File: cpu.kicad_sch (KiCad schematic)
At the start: 29 parts, among them J81 Conn_01x03_Pin, J82 Conn_Coaxial, J83 Conn_Coaxial, J84 Conn_01x02_Pin, SW81 SW_Push, SW82 SW_Push, U8 ESP32-C6-MINI-1U, U81 74HC595, U82 74HC595, U84 ISOW7842

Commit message: Put in some IO resistors.
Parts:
- added R91, R92: 100, Resistor_SMD:R_0402_1005Metric, symbol Device:R
- added R93, R94, R95, R96, R97, R98, R99: 33, Resistor_SMD:R_0402_1005Metric, symbol Device:R
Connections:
- net LATCH: now also R98.2; no longer U8.28 (IO22)
- net MOSI: now also R93.1; no longer U8.16 (IO7)
- net RX: now also R92.2; no longer U8.30 (RXD0)
- net TX: now also R91.2; no longer U8.31 (TXD0)
- net ~{CS2}: now also R94.2; no longer U8.24 (IO18)
- net ~{CS3}: now also R95.2; no longer U8.25 (IO19)
- net ~{CS4}: now also R96.2; no longer U8.26 (IO20)
- net ~{CS5}: now also R97.2; no longer U8.27 (IO21)
- net ~{LDAC}: now also R99.2; no longer U8.29 (IO23)
- new net: R97.1, U8.27 (IO21)
- new net: R93.2, U8.16 (IO7)
- new net: R94.1, U8.24 (IO18)
- new net: R99.1, U8.29 (IO23)
- new net: R91.1, U8.31 (TXD0)
- new net: R92.1, U8.30 (RXD0)
- new net: R98.1, U8.28 (IO22)
- new net: R96.1, U8.26 (IO20)
- new net: R95.1, U8.25 (IO19)
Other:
- moved on the sheet: J81, R90

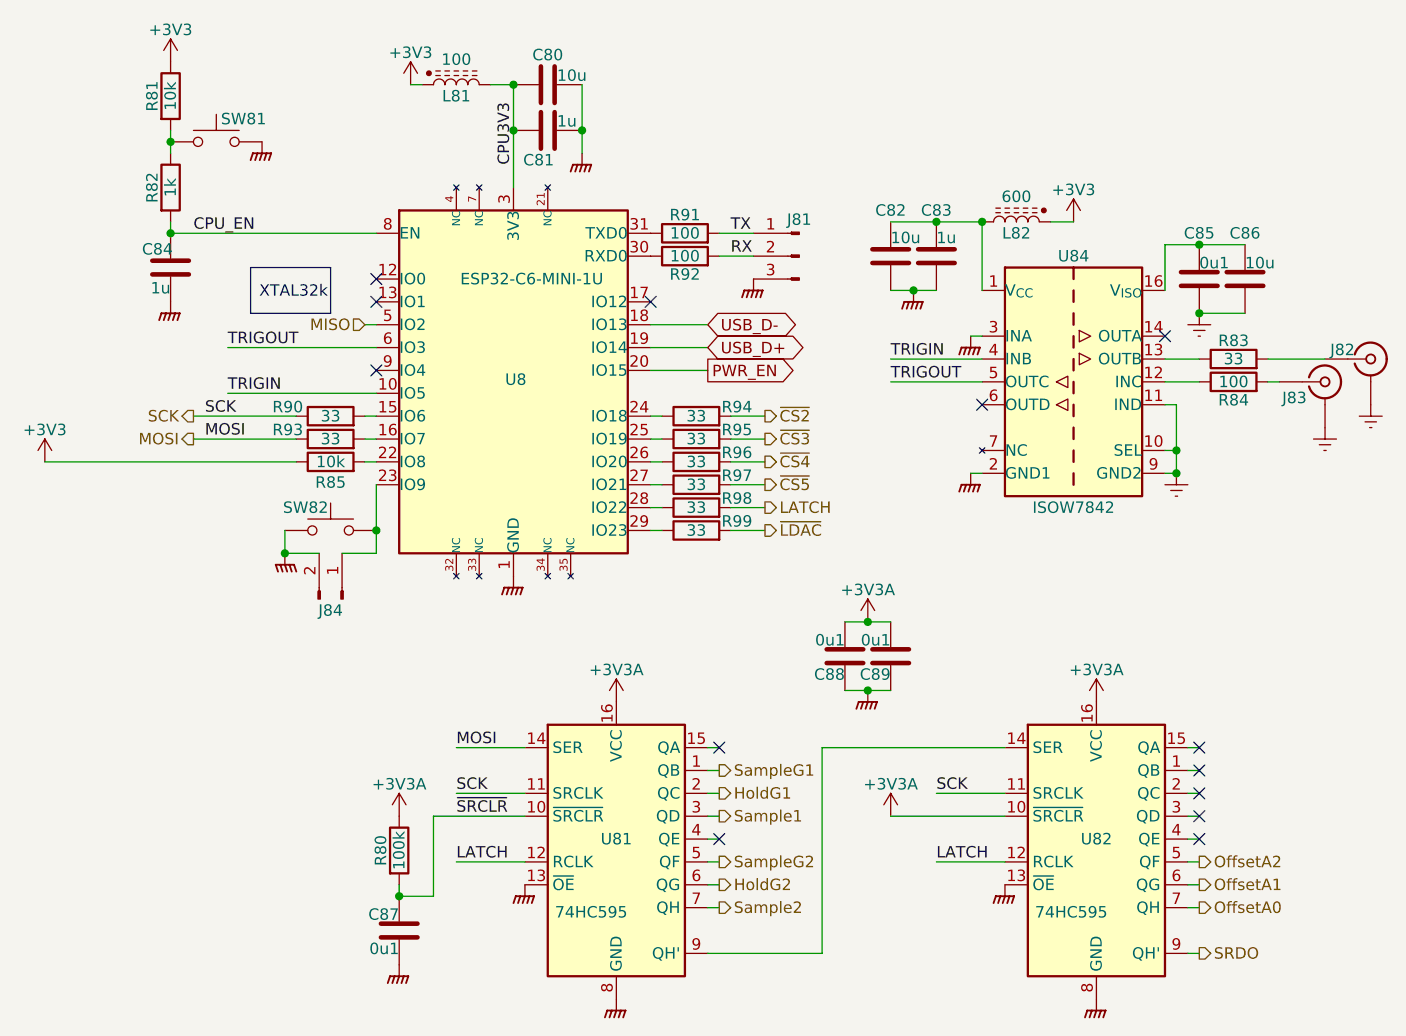
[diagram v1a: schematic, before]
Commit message: DRC update.  Repin ADC.  De-crack the S/H ground.
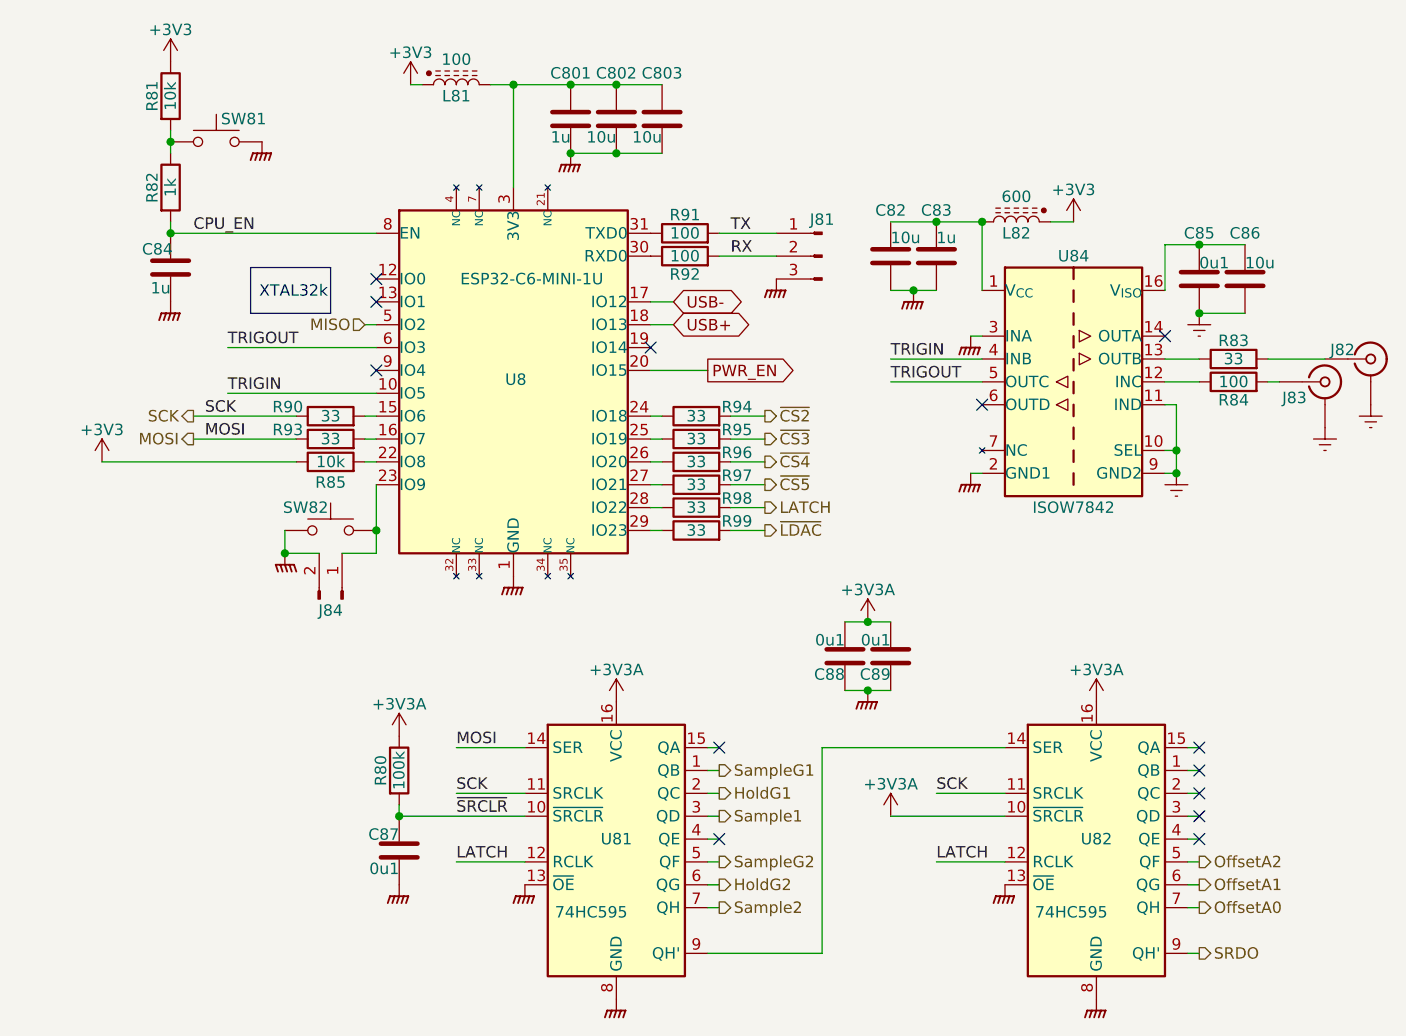
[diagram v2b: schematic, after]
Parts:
- added C803: 10u, Capacitor_SMD:C_0603_1608Metric, symbol Device:C
- renumbered C81 to C801, C80 to C802
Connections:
- net GNDPWR: now also C803.2
- net USB-: now reaches U8.17 (IO12)
- net CPU3V3: no longer names the net of C801.1, C802.1, L81.2, U8.3 (3V3)
- net CPU3V3: now also C803.1
- net USB_D+: no longer names the net of U8.19 (IO14)
- net USB_D- renamed USB+
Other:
- moved on the sheet: C801, C802, C87, J81, R80

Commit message: More component metadata.
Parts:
- C801, C802, C803, C82, C83, C84, C85, C86, C87, C88, C89, L81, L82, R80, R81, R82, R83, R84, R85, R90, R91, R92, R93, R94, R95, R96, R97, R98, R99, SW81, SW82, U8, U81, U82: Stock (none) -> JLC
- J81, J84: Stock (none) -> Heaps
- J82, J83: Stock (none) -> Bag
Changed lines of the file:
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@@
 			)
 		)
-		(property "Stock" ""
+		(property "Stock" "JLC"
 			(at 142.24 50.8 0)
 			(effects
@@
 			)
 		)
-		(property "Stock" ""
+		(property "Stock" "JLC"
 			(at 106.68 35.56 90)
 			(effects
@@
 			)
 		)
-		(property "Stock" ""
+		(property "Stock" "JLC"
 			(at 62.23 38.1 0)
 			(effects
@@
 			)
 		)
-		(property "Stock" ""
+		(property "Stock" "JLC"
 			(at 115.57 76.2 90)
 			(effects
@@
 			)
 		)
-		(property "Stock" ""
+		(property "Stock" "JLC"
 			(at 74.93 71.12 90)
 			(effects
@@
 			)
 		)
-		(property "Stock" ""
+		(property "Stock" "JLC"
 			(at 74.93 68.58 90)
 			(effects
@@
 			)
 		)
-		(property "Stock" ""
+		(property "Stock" "JLC"
 			(at 106.68 115.57 0)
 			(effects
@@
 			)
 		)
-		(property "Stock" ""
+		(property "Stock" "JLC"
 			(at 137.16 50.8 0)
 			(effects
@@
 			)
 		)
-		(property "Stock" ""
+		(property "Stock" "JLC"
 			(at 57.15 33.02 90)
 			(effects
@@
 			)
 		)
-		(property "Stock" ""
+		(property "Stock" "JLC"
 			(at 57.15 43.18 90)
 			(effects
@@
 			)
 		)
-		(property "Stock" ""
+		(property "Stock" "JLC"
 			(at 115.57 68.58 90)
 			(effects
@@
 			)
 		)
-		(property "Stock" ""
+		(property "Stock" "Bag"
 			(at 185.42 64.77 0)
 			(effects
@@
 			)
 		)
-		(property "Stock" ""
+		(property "Stock" "JLC"
 			(at 160.02 115.57 0)
 			(effects
@@
 			)
 		)
-		(property "Stock" ""
+		(property "Stock" "JLC"
 			(at 115.57 81.28 90)
 			(effects
@@
 			)
 		)
-		(property "Stock" ""
+		(property "Stock" "JLC"
 			(at 114.3 48.26 90)
 			(effects
@@
 			)
 		)
-		(property "Stock" ""
+		(property "Stock" "JLC"
 			(at 132.08 95.25 0)
 			(effects
@@
 			)
 		)
-		(property "Stock" ""
+		(property "Stock" "JLC"
 			(at 114.3 50.8 90)
 			(effects
@@
 			)
 		)
-		(property "Stock" ""
+		(property "Stock" "JLC"
 			(at 74.93 73.66 90)
 			(effects
@@
 			)
 		)
-		(property "Stock" ""
+		(property "Stock" "Bag"
 			(at 190.5 62.23 0)
 			(effects
@@
 			)
 		)
-		(property "Stock" ""
+		(property "Stock" "JLC"
 			(at 115.57 78.74 90)
 			(effects
@@
 			)
 		)
-		(property "Stock" ""
+		(property "Stock" "JLC"
 			(at 101.6 35.56 90)
 			(effects
@@
 			)
 		)
-		(property "Stock" ""
+		(property "Stock" "JLC"
 			(at 137.16 95.25 0)
 			(effects
@@
 			)
 		)
-		(property "Stock" ""
+		(property "Stock" "Heaps"
 			(at 129.54 50.8 0)
 			(effects
@@
 			)
 		)
-		(property "Stock" ""
+		(property "Stock" "JLC"
 			(at 175.26 62.23 90)
 			(effects
@@
 			)
 		)
-		(property "Stock" ""
+		(property "Stock" "JLC"
 			(at 115.57 73.66 90)
 			(effects
@@
 			)
 		)
-		(property "Stock" ""
+		(property "Stock" "JLC"
 			(at 57.15 52.07 0)
 			(effects
@@
 			)
 		)
-		(property "Stock" ""
+		(property "Stock" "JLC"
 			(at 74.93 81.28 0)
 			(effects
@@
 			)
 		)
-		(property "Stock" ""
+		(property "Stock" "JLC"
 			(at 171.45 53.34 0)
 			(effects
@@
 			)
 		)
-		(property "Stock" ""
+		(property "Stock" "Heaps"
 			(at 76.2 88.9 90)
 			(effects
@@
 			)
 		)
-		(property "Stock" ""
+		(property "Stock" "JLC"
 			(at 82.55 107.95 90)
 			(effects
@@
 			)
 		)
-		(property "Stock" ""
+		(property "Stock" "JLC"
 			(at 151.13 46.99 90)
 			(effects
@@
 			)
 		)
-		(property "Stock" ""
+		(property "Stock" "JLC"
 			(at 95.25 64.77 0)
 			(effects
@@
 			)
 		)
-		(property "Stock" ""
+		(property "Stock" "JLC"
 			(at 88.9 31.75 90)
 			(effects
@@
 			)
 		)
-		(property "Stock" ""
+		(property "Stock" "JLC"
 			(at 115.57 71.12 90)
 			(effects
@@
 			)
 		)
-		(property "Stock" ""
+		(property "Stock" "JLC"
 			(at 176.53 53.34 0)
 			(effects
@@
 			)
 		)
-		(property "Stock" ""
+		(property "Stock" "JLC"
 			(at 82.55 116.84 0)
 			(effects
@@
 			)
 		)
-		(property "Stock" ""
+		(property "Stock" "JLC"
 			(at 111.76 35.56 90)
 			(effects
@@
 			)
 		)
-		(property "Stock" ""
+		(property "Stock" "JLC"
 			(at 175.26 64.77 90)
 			(effects

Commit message: Front panel
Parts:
- added D81, D82: LED, LED_SMD:LED_0805_2012Metric, symbol Device:LED
- added R801, R802: 2k2, Resistor_SMD:R_0603_1608Metric, symbol Device:R
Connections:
- net GNDPWR: now also D81.1 (K), D82.1 (K)
- net PWR_EN: now also U8.19 (IO14); no longer U8.20 (IO15)
- net TRIGIN: now also U84.5 (OUTC); no longer U84.4 (INB)
- net TRIGOUT: now also U84.4 (INB); no longer U84.5 (OUTC)
- net Green: now reaches U8.12 (IO0)
- net Green: now also R802.1
- net SYNCMON: now reaches U8.9 (IO4)
- new net: D82.2 (A), R802.2
- new net: D81.2 (A), R801.2
- new net White: R801.1, U8.20 (IO15)
- no-connect marks 13 -> 10
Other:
- moved on the sheet: C87, R80, U81, U82

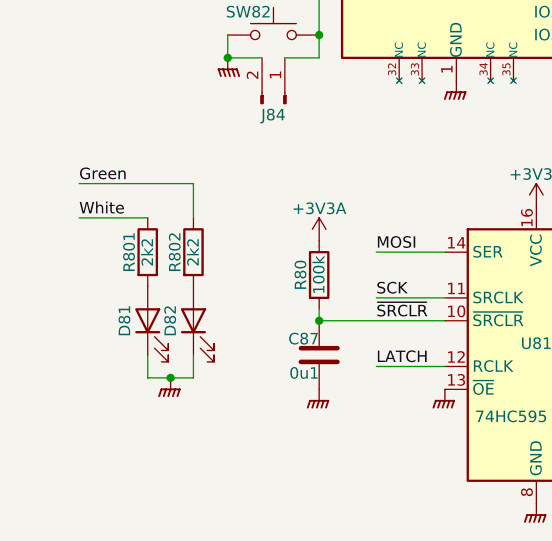
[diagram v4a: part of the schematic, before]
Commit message: Protection on ground drives.
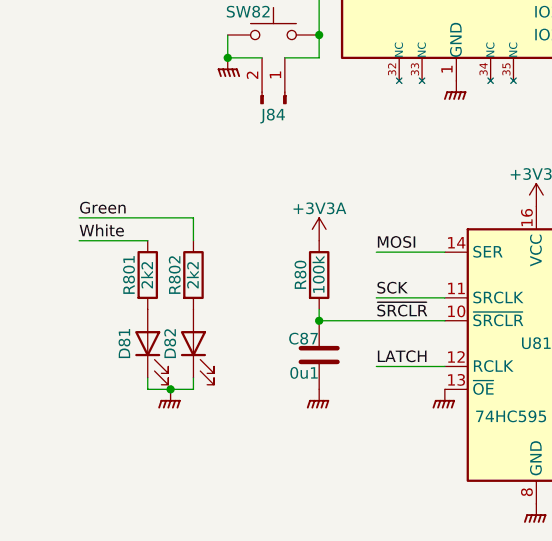
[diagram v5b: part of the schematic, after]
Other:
- moved on the sheet: D81, D82, R801, R802
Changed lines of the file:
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@@
 	)
 	(junction
-		(at 63.5 119.38)
+		(at 63.5 120.65)
 		(diameter 0)
 		(color 0 0 0 0)
@@
 	(wire
 		(pts
-			(xy 60.96 101.6) (xy 53.34 101.6)
-		)
-		(stroke
-			(width 0)
-			(type default)
-		)
-	)
-	(wire
-		(pts
 			(xy 119.38 71.12) (xy 123.19 71.12)
 		)
@@
 	(wire
 		(pts
-			(xy 53.34 97.79) (xy 66.04 97.79)
+			(xy 53.34 101.6) (xy 66.04 101.6)
 		)
 		(stroke
@@
 	(wire
 		(pts
-			(xy 60.96 119.38) (xy 63.5 119.38)
+			(xy 60.96 120.65) (xy 63.5 120.65)
 		)
 		(stroke
@@
 	(wire
 		(pts
-			(xy 66.04 116.84) (xy 66.04 119.38)
+			(xy 66.04 119.38) (xy 66.04 120.65)
 		)
 		(stroke
@@
 	(wire
 		(pts
-			(xy 63.5 119.38) (xy 66.04 119.38)
+			(xy 63.5 120.65) (xy 66.04 120.65)
 		)
 		(stroke
@@
 	(wire
 		(pts
-			(xy 66.04 101.6) (xy 66.04 97.79)
+			(xy 66.04 104.14) (xy 66.04 101.6)
 		)
 		(stroke
@@
 	(wire
 		(pts
+			(xy 53.34 104.14) (xy 60.96 104.14)
+		)
+		(stroke
+			(width 0)
+			(type default)
+		)
+	)
+	(wire
+		(pts
 			(xy 114.3 123.19) (xy 115.57 123.19)
 		)
@@
 	(wire
 		(pts
-			(xy 60.96 116.84) (xy 60.96 119.38)
+			(xy 60.96 119.38) (xy 60.96 120.65)
 		)
 		(stroke
@@
 	)
 	(label "White"
-		(at 53.34 101.6 0)
+		(at 53.34 104.14 0)
 		(effects
 			(font
@@
 	)
 	(label "Green"
-		(at 53.34 97.79 0)
+		(at 53.34 101.6 0)
 		(effects
 			(font
@@
 	(symbol
 		(lib_id "Device:LED")
-		(at 66.04 113.03 90)
+		(at 66.04 115.57 90)
 		(unit 1)
 		(exclude_from_sim no)
@@
 		(dnp no)
 		(property "Reference" "D82"
-			(at 63.5 113.03 0)
+			(at 63.5 115.57 0)
 			(effects
 				(font
@@
 		)
 		(property "Value" "LED"
-			(at 68.58 113.03 0)
+			(at 68.58 115.57 0)
 			(effects
 				(font
@@
 		)
 		(property "Footprint" "LED_SMD:LED_0805_2012Metric"
-			(at 66.04 113.03 0)
+			(at 66.04 115.57 0)
 			(effects
 				(font
@@
 		)
 		(property "Datasheet" "Green"
-			(at 66.04 113.03 0)
+			(at 66.04 115.57 0)
 			(effects
 				(font
@@
 		)
 		(property "Description" "Light emitting diode"
-			(at 66.04 113.03 0)
+			(at 66.04 115.57 0)
 			(effects
 				(font
@@
 		)
 		(property "Sim.Pins" "1=K 2=A"
-			(at 66.04 113.03 0)
+			(at 66.04 115.57 0)
 			(effects
 				(font
@@
 		)
 		(property "LCSC" "C2297"
-			(at 66.04 113.03 0)
+			(at 66.04 115.57 0)
 			(effects
 				(font
@@
 		)
 		(property "Stock" "JLC"
-			(at 66.04 113.03 0)
+			(at 66.04 115.57 0)
 			(effects
 				(font
@@
 	(symbol
 		(lib_id "Device:R")
-		(at 66.04 105.41 0)
+		(at 66.04 107.95 0)
 		(unit 1)
 		(exclude_from_sim no)
@@
 		(dnp no)
 		(property "Reference" "R802"
-			(at 64.008 105.41 90)
+			(at 64.008 107.95 90)
 			(effects
 				(font
@@
 		)
 		(property "Value" "2k2"
-			(at 66.04 105.41 90)
+			(at 66.04 107.95 90)
 			(effects
 				(font
@@
 		)
 		(property "Footprint" "Resistor_SMD:R_0603_1608Metric"
-			(at 64.262 105.41 90)
+			(at 64.262 107.95 90)
 			(effects
 				(font
@@
 		)
 		(property "Datasheet" "~"
-			(at 66.04 105.41 0)
+			(at 66.04 107.95 0)
 			(effects
 				(font
@@
 		)
 		(property "Description" "Resistor"
-			(at 66.04 105.41 0)
+			(at 66.04 107.95 0)
 			(effects
 				(font
@@
 		)
 		(property "LCSC" "C4190"
-			(at 66.04 105.41 90)
+			(at 66.04 107.95 90)
 			(effects
 				(font
@@
 		)
 		(property "Stock" "JLC"
-			(at 66.04 105.41 90)
+			(at 66.04 107.95 90)
 			(effects
 				(font
@@
 	(symbol
 		(lib_id "power:GNDPWR")
-		(at 63.5 119.38 0)
+		(at 63.5 120.65 0)
 		(unit 1)
 		(exclude_from_sim no)
@@
 		(dnp no)
 		(property "Reference" "#PWR0770"
-			(at 63.5 125.73 0)
+			(at 63.5 127 0)
 			(effects
 				(font
@@
 		)
 		(property "Value" "GNDPWR"
-			(at 63.5 122.682 0)
+			(at 63.5 123.952 0)
 			(effects
 				(font
@@
 		)
 		(property "Footprint" ""
-			(at 63.5 120.65 0)
+			(at 63.5 121.92 0)
 			(effects
 				(font
@@
 		)
 		(property "Datasheet" "~"
-			(at 63.5 120.65 0)
+			(at 63.5 121.92 0)
 			(effects
 				(font
@@
 		)
 		(property "Description" "Power symbol creates a global label with name \"GNDPWR\" , global ground"
-			(at 63.5 119.38 0)
+			(at 63.5 120.65 0)
 			(effects
 				(font
@@
 	(symbol
 		(lib_id "Device:LED")
-		(at 60.96 113.03 90)
+		(at 60.96 115.57 90)
 		(unit 1)
 		(exclude_from_sim no)
@@
 		(dnp no)
 		(property "Reference" "D81"
-			(at 58.42 113.03 0)
+			(at 58.42 115.57 0)
 			(effects
 				(font
@@
 		)
 		(property "Value" "LED"
-			(at 63.5 113.03 0)
+			(at 63.5 115.57 0)
 			(effects
 				(font
@@
 		)
 		(property "Footprint" "LED_SMD:LED_0805_2012Metric"
-			(at 60.96 113.03 0)
+			(at 60.96 115.57 0)
 			(effects
 				(font
@@
 		)
 		(property "Datasheet" "White"
-			(at 60.96 113.03 0)
+			(at 60.96 115.57 0)
 			(effects
 				(font
@@
 		)
 		(property "Description" "Light emitting diode"
-			(at 60.96 113.03 0)
+			(at 60.96 115.57 0)
 			(effects
 				(font
@@
 		)
 		(property "Sim.Pins" "1=K 2=A"
-			(at 60.96 113.03 0)
+			(at 60.96 115.57 0)
 			(effects
 				(font
@@
 		)
 		(property "LCSC" "C34499"
-			(at 60.96 113.03 0)
+			(at 60.96 115.57 0)
 			(effects
 				(font
@@
 		)
 		(property "Stock" "JLC"
-			(at 60.96 113.03 0)
+			(at 60.96 115.57 0)
 			(effects
 				(font
@@
 	(symbol
 		(lib_id "Device:R")
-		(at 60.96 105.41 0)
+		(at 60.96 107.95 0)
 		(unit 1)
 		(exclude_from_sim no)
@@
 		(dnp no)
 		(property "Reference" "R801"
-			(at 58.928 105.41 90)
+			(at 58.928 107.95 90)
 			(effects
 				(font
@@
 		)
 		(property "Value" "2k2"
-			(at 60.96 105.41 90)
+			(at 60.96 107.95 90)
 			(effects
 				(font
@@
 		)
 		(property "Footprint" "Resistor_SMD:R_0603_1608Metric"
-			(at 59.182 105.41 90)
+			(at 59.182 107.95 90)
 			(effects
 				(font
@@
 		)
 		(property "Datasheet" "~"
-			(at 60.96 105.41 0)
+			(at 60.96 107.95 0)
 			(effects
 				(font
@@
 		)
 		(property "Description" "Resistor"
-			(at 60.96 105.41 0)
+			(at 60.96 107.95 0)
 			(effects
 				(font
@@
 		)
 		(property "LCSC" "C4190"
-			(at 60.96 105.41 90)
+			(at 60.96 107.95 90)
 			(effects
 				(font
@@
 		)
 		(property "Stock" "JLC"
-			(at 60.96 105.41 90)
+			(at 60.96 107.95 90)
 			(effects
 				(font

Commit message: Capacitor tweak.
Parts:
- C82, C86: value 10u -> 22u; footprint Capacitor_SMD:C_0603_1608Metric -> Capacitor_SMD:C_0805_2012Metric; LCSC C96446 -> C45783
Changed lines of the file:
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@@
 			)
 		)
-		(property "Value" "10u"
+		(property "Value" "22u"
 			(at 137.16 48.768 0)
 			(effects
@@
 			)
 		)
-		(property "Footprint" "Capacitor_SMD:C_0603_1608Metric"
+		(property "Footprint" "Capacitor_SMD:C_0805_2012Metric"
 			(at 138.1252 54.61 0)
 			(effects
@@
 			)
 		)
-		(property "LCSC" "C96446"
+		(property "LCSC" "C45783"
 			(at 137.16 50.8 0)
 			(effects
@@
 			)
 		)
-		(property "Value" "10u"
+		(property "Value" "22u"
 			(at 176.53 51.562 0)
 			(effects
@@
 			)
 		)
-		(property "Footprint" "Capacitor_SMD:C_0603_1608Metric"
+		(property "Footprint" "Capacitor_SMD:C_0805_2012Metric"
 			(at 177.4952 57.15 0)
 			(effects
@@
 			)
 		)
-		(property "LCSC" "C96446"
+		(property "LCSC" "C45783"
 			(at 176.53 53.34 0)
 			(effects
